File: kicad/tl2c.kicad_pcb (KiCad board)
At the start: 4 copper layers, 104.1 x 50.8 mm, 84 parts, among them IC101 ATTINY20-X, P101 12VDC, P102 I2C Master, P103 Spare, P104 ISP Header, P105 LED_DRIVER, P106 240VAC, P107 LED_DRIVER, P108 LED_OUT, P301 PIR13, Q301 IRLML2502, Q302 IRLML2502, Q303 IRLML2502, Q401 IRLML2502, Q402 IRLML2502, Q403 IRLML2502, SW101 TL3315NF160Q, U201 LF120ABDT-TR, U202 TPS70933

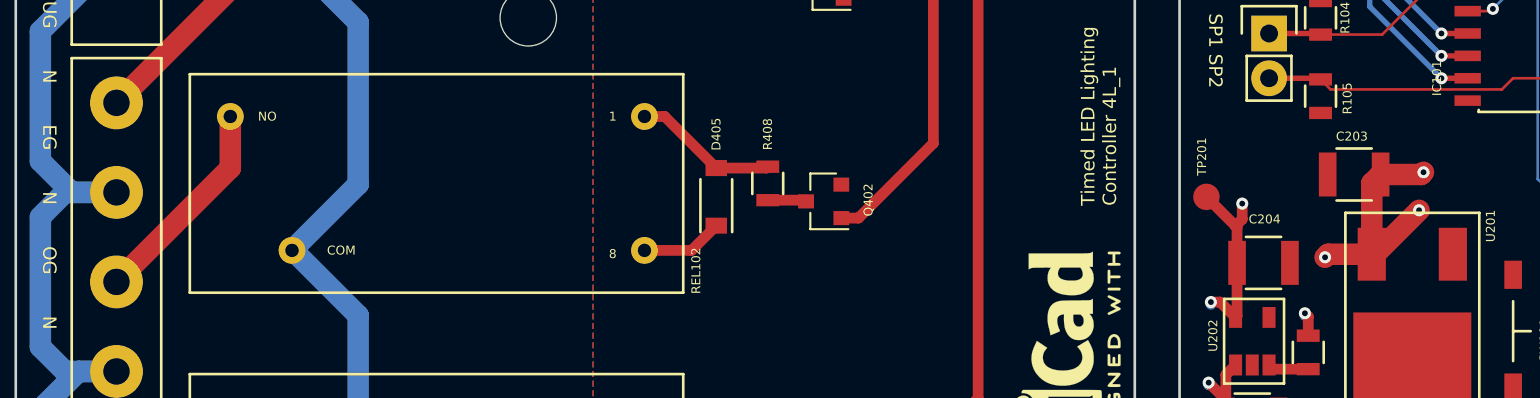
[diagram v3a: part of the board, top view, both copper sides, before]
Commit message: Some part changes due to sourcing
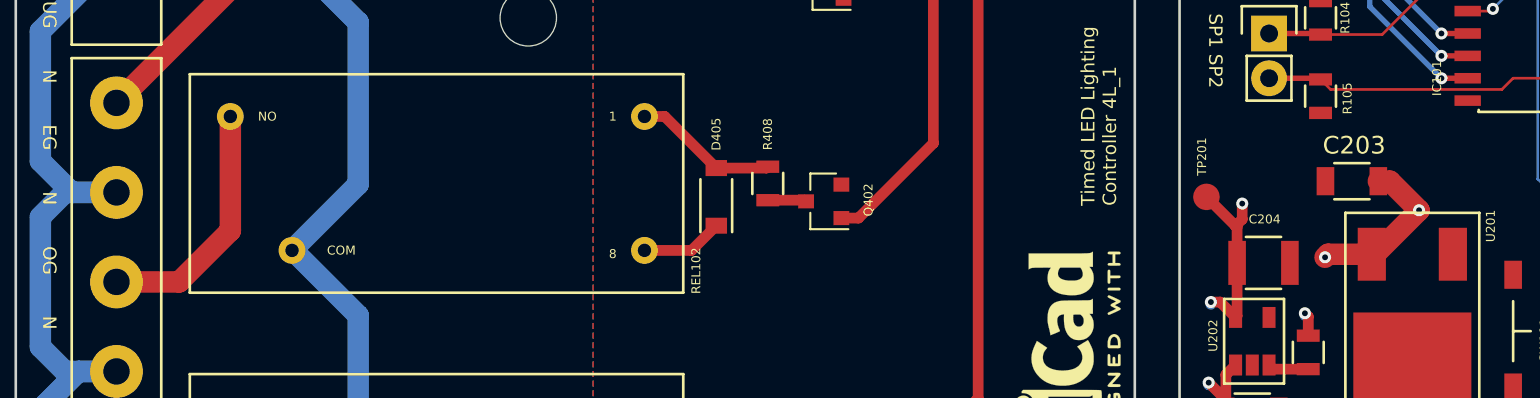
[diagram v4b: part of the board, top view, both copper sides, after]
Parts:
- C203: footprint Capacitors_SMD:C_1210 -> Capacitors_SMD:C_1206
- moved C203 0.40 mm to (157.1, 50.9)
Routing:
- net /PIR13/U+: track 41.9 -> 37.7 mm, vias 6 -> 5
- net /LineEG: track 12.1 -> 14.1 mm
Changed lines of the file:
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@@
     (thickness 1.6)
     (drawings 28)
-    (tracks 356)
+    (tracks 354)
     (zones 0)
     (modules 84)
@@
   )
   (setup
-    (last_trace_width 0.6096)
+    (last_trace_width 1.2192)
     (user_trace_width 0.3048)
     (user_trace_width 0.6096)
@@
   )
   (module Capacitors_SMD:C_1210 (layer F.Cu)
-    (at 157.226 50.546 180)
-    (descr "Capacitor SMD 1210, reflow soldering, AVX (see smccp.pdf)")
-    (tags "capacitor 1210")
-    (attr smd)
-    (fp_text reference C203 (at 0.127 2.159 180) (layer F.SilkS)
-      (effects (font (size 0.508 0.508) (thickness 0.127)))
-    )
-    (fp_text value "2.2μF 50V" (at 0 2.7 180) (layer F.Fab)
-      (effects (font (size 0.508 0.508) (thickness 0.127)))
-    )
-    (fp_line (start -1.6 1.25) (end -1.6 -1.25) (layer F.Fab) (width 0.15))
-    (fp_line (start 1.6 1.25) (end -1.6 1.25) (layer F.Fab) (width 0.15))
-    (fp_line (start 1.6 -1.25) (end 1.6 1.25) (layer F.Fab) (width 0.15))
-    (fp_line (start -1.6 -1.25) (end 1.6 -1.25) (layer F.Fab) (width 0.15))
-    (fp_line (start -2.3 -1.6) (end 2.3 -1.6) (layer F.CrtYd) (width 0.05))
-    (fp_line (start -2.3 1.6) (end 2.3 1.6) (layer F.CrtYd) (width 0.05))
-    (fp_line (start -2.3 -1.6) (end -2.3 1.6) (layer F.CrtYd) (width 0.05))
-    (fp_line (start 2.3 -1.6) (end 2.3 1.6) (layer F.CrtYd) (width 0.05))
-    (fp_line (start 1 -1.475) (end -1 -1.475) (layer F.SilkS) (width 0.15))
-    (fp_line (start -1 1.475) (end 1 1.475) (layer F.SilkS) (width 0.15))
-    (pad 1 smd rect (at -1.5 0 180) (size 1 2.5) (layers F.Cu F.Paste F.Mask)
-      (net 35 /PIR13/U+))
-    (pad 2 smd rect (at 1.5 0 180) (size 1 2.5) (layers F.Cu F.Paste F.Mask)
-      (net 1 GND))
-    (model Capacitors_SMD.3dshapes/C_1210.wrl
-      (at (xyz 0 0 0))
-      (scale (xyz 1 1 1))
-      (rotate (xyz 0 0 0))
-    )
-  )
-  (module Capacitors_SMD:C_1210 (layer F.Cu)
     (at 152.0825 55.5625)
     (descr "Capacitor SMD 1210, reflow soldering, AVX (see smccp.pdf)")
@@
     (pad 1 np_thru_hole circle (at 0 0) (size 3.2 3.2) (drill 3.2) (layers *.Cu *.Mask))
   )
+  (module Capacitors_SMD:C_1206 (layer F.Cu)
+    (at 157.099 50.927 180)
+    (descr "Capacitor SMD 1206, reflow soldering, AVX (see smccp.pdf)")
+    (tags "capacitor 1206")
+    (attr smd)
+    (fp_text reference C203 (at -0.127 2.032 180) (layer F.SilkS)
+      (effects (font (size 1 1) (thickness 0.15)))
+    )
+    (fp_text value "2.2μF 50V" (at 0 2.3 180) (layer F.Fab)
+      (effects (font (size 1 1) (thickness 0.15)))
+    )
+    (fp_line (start -1.6 0.8) (end -1.6 -0.8) (layer F.Fab) (width 0.15))
+    (fp_line (start 1.6 0.8) (end -1.6 0.8) (layer F.Fab) (width 0.15))
+    (fp_line (start 1.6 -0.8) (end 1.6 0.8) (layer F.Fab) (width 0.15))
+    (fp_line (start -1.6 -0.8) (end 1.6 -0.8) (layer F.Fab) (width 0.15))
+    (fp_line (start -2.3 -1.15) (end 2.3 -1.15) (layer F.CrtYd) (width 0.05))
+    (fp_line (start -2.3 1.15) (end 2.3 1.15) (layer F.CrtYd) (width 0.05))
+    (fp_line (start -2.3 -1.15) (end -2.3 1.15) (layer F.CrtYd) (width 0.05))
+    (fp_line (start 2.3 -1.15) (end 2.3 1.15) (layer F.CrtYd) (width 0.05))
+    (fp_line (start 1 -1.025) (end -1 -1.025) (layer F.SilkS) (width 0.15))
+    (fp_line (start -1 1.025) (end 1 1.025) (layer F.SilkS) (width 0.15))
+    (pad 1 smd rect (at -1.5 0 180) (size 1 1.6) (layers F.Cu F.Paste F.Mask)
+      (net 35 /PIR13/U+))
+    (pad 2 smd rect (at 1.5 0 180) (size 1 1.6) (layers F.Cu F.Paste F.Mask)
+      (net 1 GND))
+    (model Capacitors_SMD.3dshapes/C_1206.wrl
+      (at (xyz 0 0 0))
+      (scale (xyz 1 1 1))
+      (rotate (xyz 0 0 0))
+    )
+  )
   (gr_text "Timed LED Lighting \nController 4L_1" (at 171.958 28.575) (layer F.SilkS)
     (effects (font (size 0.762 0.762) (thickness 0.127)) (justify left))
@@
   (segment (start 94.853 28.204) (end 94.853 38.624) (width 1.2192) (layer F.Cu) (net 22))
   (segment (start 94.853 38.624) (end 86.995 46.482) (width 1.2192) (layer F.Cu) (net 22))
-  (segment (start 93.456 47.254) (end 93.456 50.181) (width 1.2192) (layer F.Cu) (net 23))
-  (segment (start 93.456 50.181) (end 86.995 56.642) (width 1.2192) (layer F.Cu) (net 23))
+  (segment (start 93.456 47.254) (end 93.456 53.737) (width 1.2192) (layer F.Cu) (net 23) (status 400000))
+  (segment (start 90.551 56.642) (end 86.995 56.642) (width 1.2192) (layer F.Cu) (net 23) (status 800000))
+  (segment (start 93.456 53.737) (end 90.551 56.642) (width 1.2192) (layer F.Cu) (net 23))
   (segment (start 93.456 64.272) (end 90.926 66.802) (width 1.2192) (layer F.Cu) (net 24))
   (segment (start 90.926 66.802) (end 86.995 66.802) (width 1.2192) (layer F.Cu) (net 24))
@@
   (segment (start 156.845 32.639) (end 155.575 33.909) (width 0.3048) (layer F.Cu) (net 34))
   (segment (start 155.575 33.909) (end 152.81402 33.909) (width 0.3048) (layer F.Cu) (net 34))
+  (segment (start 158.599 50.927) (end 159.258 50.927) (width 1.2192) (layer F.Cu) (net 35) (status 400000))
+  (via (at 160.909 52.578) (size 0.6858) (drill 0.3302) (layers F.Cu B.Cu) (net 35))
+  (segment (start 160.909 52.578) (end 158.415 55.072) (width 1.2192) (layer F.Cu) (net 35))
+  (segment (start 159.258 50.927) (end 160.909 52.578) (width 1.2192) (layer F.Cu) (net 35))
   (segment (start 158.228 55.072) (end 155.748 55.072) (width 1.2192) (layer F.Cu) (net 35))
   (via (at 155.575 55.245) (size 0.6858) (drill 0.3302) (layers F.Cu B.Cu) (net 35))
   (segment (start 155.748 55.072) (end 155.575 55.245) (width 1.2192) (layer F.Cu) (net 35))
   (segment (start 158.228 55.072) (end 158.415 55.072) (width 1.2192) (layer F.Cu) (net 35))
-  (segment (start 158.415 55.072) (end 160.909 52.578) (width 1.2192) (layer F.Cu) (net 35))
-  (via (at 160.909 52.578) (size 0.6858) (drill 0.3302) (layers F.Cu B.Cu) (net 35))
-  (segment (start 158.726 50.546) (end 161.036 50.546) (width 1.2192) (layer F.Cu) (net 35))
-  (via (at 161.163 50.419) (size 0.6858) (drill 0.3302) (layers F.Cu B.Cu) (net 35))
-  (segment (start 161.036 50.546) (end 161.163 50.419) (width 1.2192) (layer F.Cu) (net 35))
-  (segment (start 158.228 55.072) (end 158.228 51.044) (width 1.2192) (layer F.Cu) (net 35))
-  (segment (start 158.228 51.044) (end 158.726 50.546) (width 1.2192) (layer F.Cu) (net 35))
   (segment (start 149.9475 64.4525) (end 149.9475 63.3335) (width 0.6096) (layer F.Cu) (net 35))
   (segment (start 149.9475 63.3335) (end 148.971 62.357) (width 0.6096) (layer F.Cu) (net 35))
@@
   (segment (start 179.385 50.8) (end 178.75 51.435) (width 0.6096) (layer F.Cu) (net 35))
   (segment (start 178.75 43.18) (end 181.61 43.18) (width 0.6096) (layer F.Cu) (net 35))
-  (segment (start 168.91 48.022) (end 170.037 48.022) (width 0.6096) (layer F.Cu) (net 36) (status 400000))
+  (segment (start 168.91 48.022) (end 170.037 48.022) (width 0.6096) (layer F.Cu) (net 36))
   (via (at 170.688 47.371) (size 0.6858) (drill 0.3302) (layers F.Cu B.Cu) (net 36))
   (segment (start 170.037 48.022) (end 170.688 47.371) (width 0.6096) (layer F.Cu) (net 36))
-  (segment (start 169.07 46.355) (end 169.07 47.862) (width 0.6096) (layer F.Cu) (net 36) (status C00000))
-  (segment (start 169.07 47.862) (end 168.91 48.022) (width 0.6096) (layer F.Cu) (net 36) (status C00000))
+  (segment (start 169.07 46.355) (end 169.07 47.862) (width 0.6096) (layer F.Cu) (net 36))
+  (segment (start 169.07 47.862) (end 168.91 48.022) (width 0.6096) (layer F.Cu) (net 36))
   (segment (start 171.196 50.861) (end 171.196 51.562) (width 0.3048) (layer F.Cu) (net 36))
   (via (at 170.561 52.197) (size 0.6858) (drill 0.3302) (layers F.Cu B.Cu) (net 36))

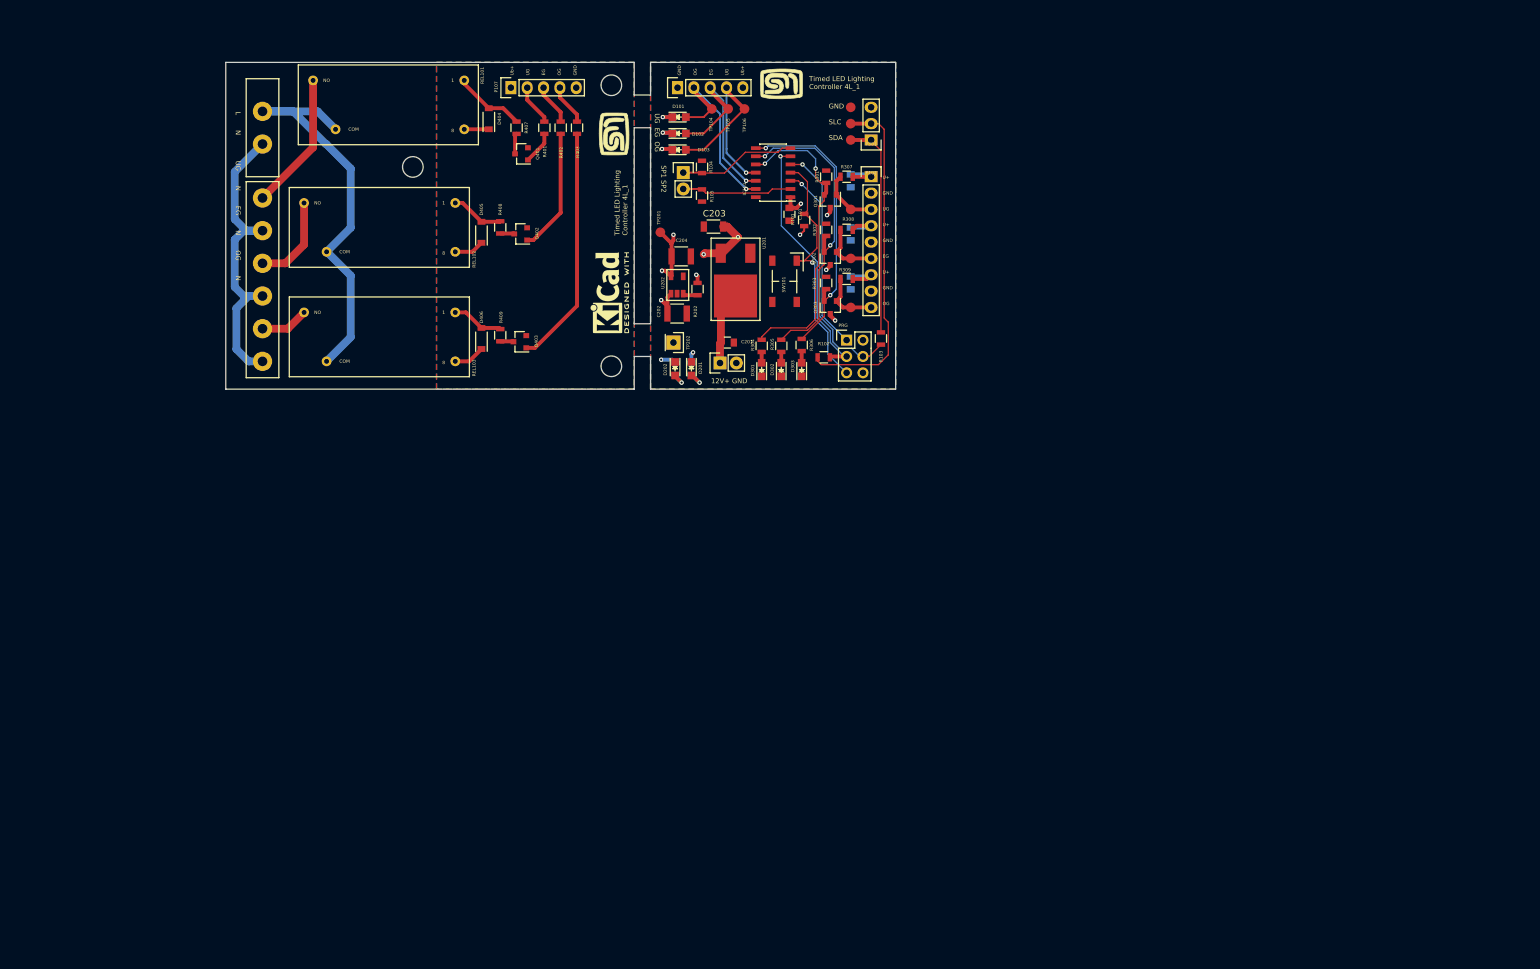
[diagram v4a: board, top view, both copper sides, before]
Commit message: Revamped the master pcb layout for the mounting holes and the actual footprint for the terminal blocks
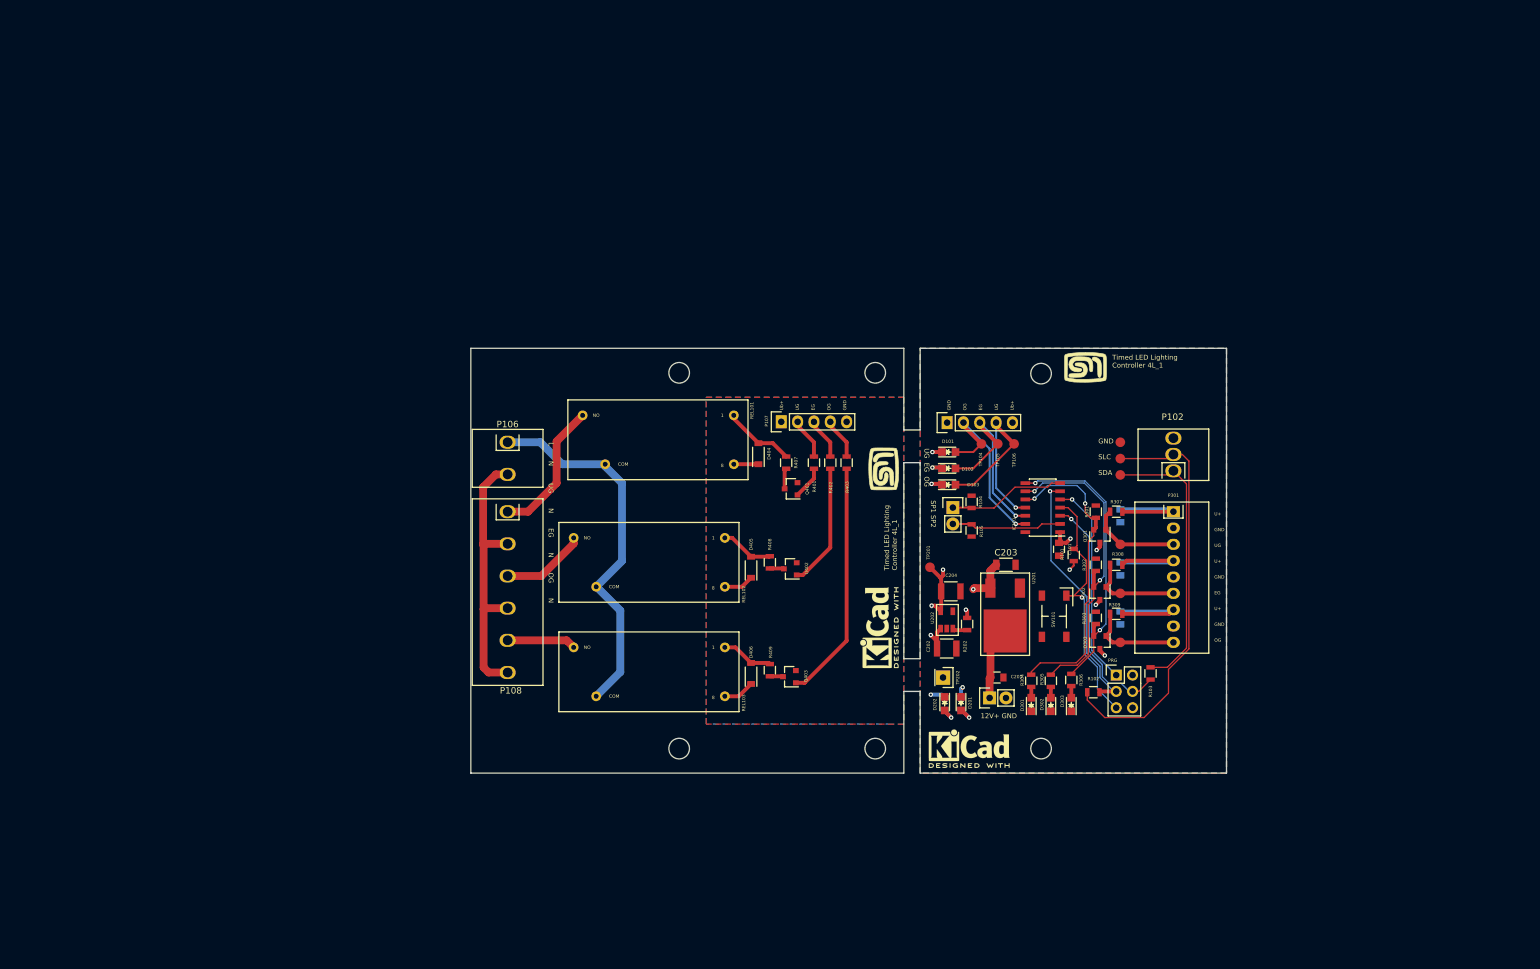
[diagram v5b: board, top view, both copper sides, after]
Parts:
- added REF**: MountingHole_3.2mm_M3, Mounting_Holes:MountingHole_3.2mm_M3, F.Cu at (151.8, 132.1)
- added REF**: MountingHole_3.2mm_M3, Mounting_Holes:MountingHole_3.2mm_M3, F.Cu at (208.0, 73.8)
- added REF**: MountingHole_3.2mm_M3, Mounting_Holes:MountingHole_3.2mm_M3, F.Cu at (208.0, 132.1)
- added REF***: KiCad-Logo2_6mm_SilkScreen, Symbols:KiCad-Logo2_6mm_SilkScreen, F.Cu at (196.8, 132.1)
- P102: footprint Pin_Headers:Pin_Header_Straight_1x03 -> tl2c-footprint:Spring_Terminal_Block_1_x_3
- P106: footprint tl2c-footprint:Pin_Header_1_x_2_5mmPitch -> tl2c-footprint:Spring_Terminal_Block_1_x_2_5mm
- P108: footprint tl2c-footprint:Pin_Header_1_x_6_54mmPitch -> tl2c-footprint:Spring_Terminal_Block_1_x_6_5mm
- P301: footprint Pin_Headers:Pin_Header_Straight_1x09 -> tl2c-footprint:Spring_Terminal_Block_1_x_9
- moved REF** 72.2 mm to (182.2, 132.1)
- moved P301 70.1 mm to (228.6, 95.2)
- moved P102 69.7 mm to (228.6, 88.9)
- moved C203 69.5 mm to (202.6, 103.5), turned to 0 degrees
- moved D101 66.8 mm to (193.7, 86.0)
- moved D102 66.8 mm to (193.7, 88.5)
- moved D103 66.8 mm to (193.7, 91.1)
- moved R103 66.8 mm to (225.0, 120.4)
- moved R106 66.8 mm to (193.7, 86.0)
- moved R107 66.8 mm to (193.7, 88.5)
- moved R108 66.8 mm to (193.7, 91.1)
- moved R305 66.8 mm to (209.6, 121.5)
- moved C101 66.8 mm to (210.8, 101.1)
- moved C302 66.8 mm to (220.3, 104.1)
- moved D201 66.8 mm to (195.6, 125.1)
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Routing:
- net /PIR13/U+: track 37.7 -> 65.7 mm, vias 5 -> 4
- net /SCL: track 53.5 -> 66.0 mm
- net /SDA: track 33.7 -> 43.7 mm
- net /Neutral: track 51.7 -> 44.4 mm
- net /Lin: track 64.5 -> 58.4 mm
- net /PIR13/PIR_EG: track 9.52 -> 14.6 mm
- net /PIR13/PIR_UG: track 9.44 -> 14.5 mm
- net /PIR13/PIR_OG: track 9.52 -> 14.6 mm
- net /LineOG: track 7.51 -> 10.7 mm
- net /LineEG: track 14.1 -> 13.2 mm
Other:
- board size 104.1 x 50.8 mm -> 117.5 x 66 mm

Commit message: Corrected the Ub+ to the LV board... should be U+
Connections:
- P105 pad 1: /PIR13/Ub+ -> /PIR13/U+
- SW101 pad 2: Net-(SW101-Pad2) -> (no net)
- SW101 pad 4: Net-(SW101-Pad4) -> (no net)
- U202 pad 4: Net-(U202-Pad4) -> (no net)
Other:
- board text added: "GND OG EG UG U+"
- board text added: "U+ UG EG OG GND"
- board text removed: "GND OG EG UG Ub+"
- board text removed: "Ub+ UG EG OG GND"
